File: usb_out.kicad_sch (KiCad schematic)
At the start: 31 parts, among them J6 USB_C_Receptacle_USB2.0, Q22 2N7002, U12 SY8105, U13 LM75B, U14 INA219AxD

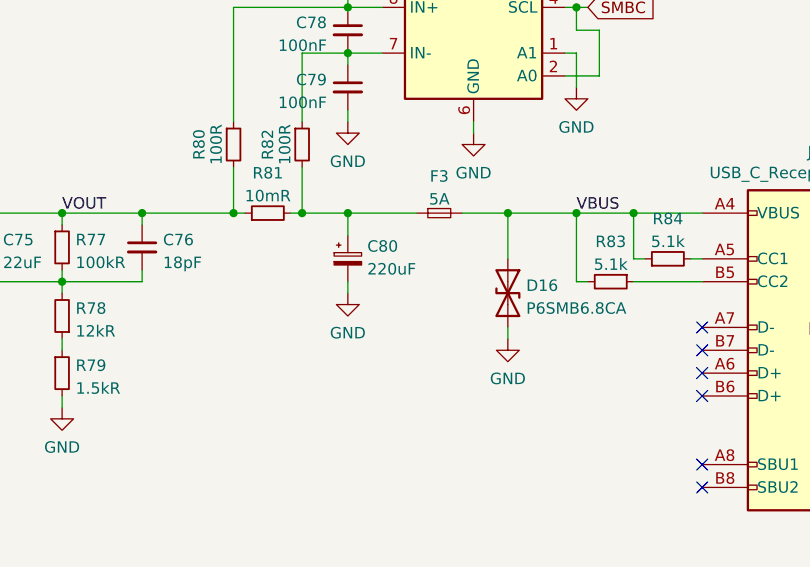
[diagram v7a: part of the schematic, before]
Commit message: Add more voltage rail LEDs
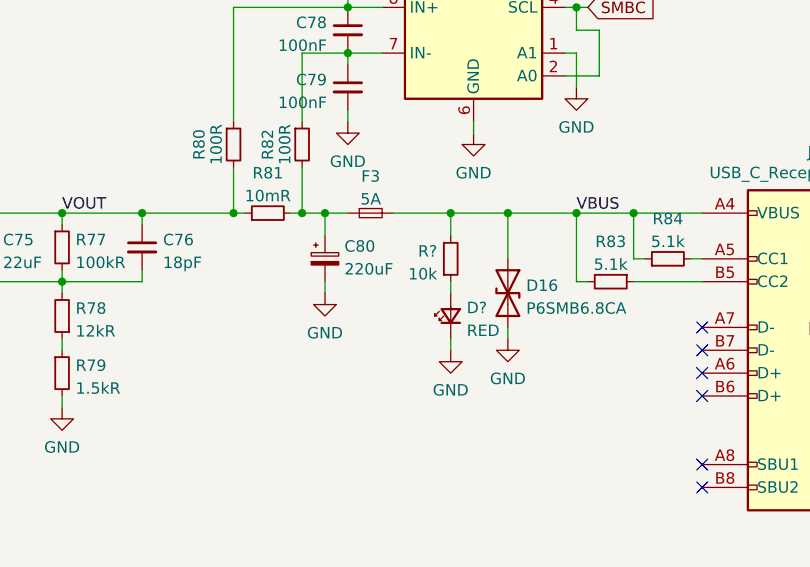
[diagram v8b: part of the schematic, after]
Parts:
- added D?: RED, LED_SMD:LED_0603_1608Metric, symbol Device:LED_Small
- added R?: 10k, Resistor_SMD:R_0402_1005Metric, symbol Device:R_Small
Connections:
- net GND: now also D?.1 (K)
- net VBUS: now also R?.2
- new net: D?.2 (A), R?.1
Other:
- moved on the sheet: C80, F3
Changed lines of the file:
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@@
   (junction (at 179.07 66.04) (diameter 0) (color 0 0 0 0)
   )
+  (junction (at 158.75 66.04) (diameter 0) (color 0 0 0 0)
+  )
   (junction (at 115.57 66.04) (diameter 0) (color 0 0 0 0)
   )
@@
   (junction (at 134.62 66.04) (diameter 0) (color 0 0 0 0)
   )
-  (junction (at 147.32 66.04) (diameter 0) (color 0 0 0 0)
-  )
   (junction (at 161.29 34.29) (diameter 0) (color 0 0 0 0)
   )
@@
   )
   (junction (at 97.79 66.04) (diameter 0) (color 0 0 0 0)
+  )
+  (junction (at 144.78 66.04) (diameter 0) (color 0 0 0 0)
   )
   (junction (at 209.55 113.03) (diameter 0) (color 0 0 0 0)
@@
     (stroke (width 0) (type default) (color 0 0 0 0))
   )
-  (wire (pts (xy 147.32 73.66) (xy 147.32 74.93))
+  (wire (pts (xy 144.78 73.66) (xy 144.78 74.93))
     (stroke (width 0) (type default) (color 0 0 0 0))
   )
@@
     (stroke (width 0) (type default) (color 0 0 0 0))
   )
-  (wire (pts (xy 147.32 66.04) (xy 154.94 66.04))
-    (stroke (width 0) (type default) (color 0 0 0 0))
-  )
   (wire (pts (xy 52.07 66.04) (xy 53.34 66.04))
     (stroke (width 0) (type default) (color 0 0 0 0))
@@
     (stroke (width 0) (type default) (color 0 0 0 0))
   )
+  (wire (pts (xy 158.75 66.04) (xy 165.1 66.04))
+    (stroke (width 0) (type default) (color 0 0 0 0))
+  )
   (wire (pts (xy 172.72 45.72) (xy 172.72 43.18))
     (stroke (width 0) (type default) (color 0 0 0 0))
@@
     (stroke (width 0) (type default) (color 0 0 0 0))
   )
-  (wire (pts (xy 142.24 66.04) (xy 147.32 66.04))
+  (wire (pts (xy 142.24 66.04) (xy 144.78 66.04))
     (stroke (width 0) (type default) (color 0 0 0 0))
   )
@@
     (stroke (width 0) (type default) (color 0 0 0 0))
   )
-  (wire (pts (xy 160.02 66.04) (xy 165.1 66.04))
+  (wire (pts (xy 152.4 66.04) (xy 158.75 66.04))
     (stroke (width 0) (type default) (color 0 0 0 0))
   )
@@
     (stroke (width 0) (type default) (color 0 0 0 0))
   )
+  (wire (pts (xy 158.75 73.66) (xy 158.75 74.93))
+    (stroke (width 0) (type default) (color 0 0 0 0))
+  )
   (wire (pts (xy 158.75 34.29) (xy 161.29 34.29))
     (stroke (width 0) (type default) (color 0 0 0 0))
@@
     (stroke (width 0) (type default) (color 0 0 0 0))
   )
-  (wire (pts (xy 147.32 66.04) (xy 147.32 68.58))
+  (wire (pts (xy 144.78 66.04) (xy 144.78 68.58))
     (stroke (width 0) (type default) (color 0 0 0 0))
   )
@@
     (stroke (width 0) (type default) (color 0 0 0 0))
   )
+  (wire (pts (xy 158.75 80.01) (xy 158.75 81.28))
+    (stroke (width 0) (type default) (color 0 0 0 0))
+  )
   (wire (pts (xy 147.32 41.91) (xy 147.32 43.18))
     (stroke (width 0) (type default) (color 0 0 0 0))
@@
     (stroke (width 0) (type default) (color 0 0 0 0))
   )
+  (wire (pts (xy 158.75 68.58) (xy 158.75 66.04))
+    (stroke (width 0) (type default) (color 0 0 0 0))
+  )
   (wire (pts (xy 115.57 66.04) (xy 124.46 66.04))
     (stroke (width 0) (type default) (color 0 0 0 0))
@@
   )
   (wire (pts (xy 172.72 48.26) (xy 171.45 48.26))
+    (stroke (width 0) (type default) (color 0 0 0 0))
+  )
+  (wire (pts (xy 144.78 66.04) (xy 147.32 66.04))
     (stroke (width 0) (type default) (color 0 0 0 0))
   )
@@
     (pin "1")
   )
-  (symbol (lib_id "Device:Fuse_Small") (at 157.48 66.04 0) (unit 1)
-    (in_bom yes) (on_board yes) (fields_autoplaced)
-    (property "Reference" "F3" (id 0) (at 157.48 61.9592 0))
-    (property "Value" "5A" (id 1) (at 157.48 64.4961 0))
-    (property "Footprint" "Fuse:Fuse_1206_3216Metric" (id 2) (at 157.48 66.04 0)
-      (effects (font (size 1.27 1.27)) hide)
-    )
-    (property "Datasheet" "https://datasheet.lcsc.com/lcsc/1912111437_HOLLY-12T-050L2_C377290.pdf" (id 3) (at 157.48 66.04 0)
-      (effects (font (size 1.27 1.27)) hide)
-    )
-    (property "LCSC" "C377290" (id 4) (at 157.48 66.04 0)
+  (symbol (lib_id "Device:Fuse_Small") (at 149.86 66.04 0) (unit 1)
+    (in_bom yes) (on_board yes) (fields_autoplaced)
+    (property "Reference" "F3" (id 0) (at 149.86 61.9592 0))
+    (property "Value" "5A" (id 1) (at 149.86 64.4961 0))
+    (property "Footprint" "Fuse:Fuse_1206_3216Metric" (id 2) (at 149.86 66.04 0)
+      (effects (font (size 1.27 1.27)) hide)
+    )
+    (property "Datasheet" "https://datasheet.lcsc.com/lcsc/1912111437_HOLLY-12T-050L2_C377290.pdf" (id 3) (at 149.86 66.04 0)
+      (effects (font (size 1.27 1.27)) hide)
+    )
+    (property "LCSC" "C377290" (id 4) (at 149.86 66.04 0)
       (effects (font (size 1.27 1.27)) hide)
     )
@@
     (pin "1")
   )
-  (symbol (lib_id "power:GND") (at 147.32 74.93 0) (unit 1)
-    (in_bom yes) (on_board yes) (fields_autoplaced)
-    (property "Reference" "#PWR0234" (id 0) (at 147.32 81.28 0)
-      (effects (font (size 1.27 1.27)) hide)
-    )
-    (property "Value" "GND" (id 1) (at 147.32 79.3734 0))
-    (property "Footprint" "" (id 2) (at 147.32 74.93 0)
-      (effects (font (size 1.27 1.27)) hide)
-    )
-    (property "Datasheet" "" (id 3) (at 147.32 74.93 0)
+  (symbol (lib_id "power:GND") (at 144.78 74.93 0) (unit 1)
+    (in_bom yes) (on_board yes) (fields_autoplaced)
+    (property "Reference" "#PWR0234" (id 0) (at 144.78 81.28 0)
+      (effects (font (size 1.27 1.27)) hide)
+    )
+    (property "Value" "GND" (id 1) (at 144.78 79.3734 0))
+    (property "Footprint" "" (id 2) (at 144.78 74.93 0)
+      (effects (font (size 1.27 1.27)) hide)
+    )
+    (property "Datasheet" "" (id 3) (at 144.78 74.93 0)
       (effects (font (size 1.27 1.27)) hide)
     )
@@
     (pin "1")
   )
+  (symbol (lib_id "Device:R_Small") (at 158.75 71.12 0) (mirror x) (unit 1)
+    (in_bom yes) (on_board yes) (fields_autoplaced)
+    (property "Reference" "R?" (id 0) (at 157.2515 70.2853 0)
+      (effects (font (size 1.27 1.27)) (justify right))
+    )
+    (property "Value" "10k" (id 1) (at 157.2515 72.8222 0)
+      (effects (font (size 1.27 1.27)) (justify right))
+    )
+    (property "Footprint" "Resistor_SMD:R_0402_1005Metric" (id 2) (at 158.75 71.12 0)
+      (effects (font (size 1.27 1.27)) hide)
+    )
+    (property "Datasheet" "~" (id 3) (at 158.75 71.12 0)
+      (effects (font (size 1.27 1.27)) hide)
+    )
+    (property "LCSC" "C25744" (id 4) (at 158.75 71.12 0)
+      (effects (font (size 1.27 1.27)) hide)
+    )
+    (pin "1")
+    (pin "2")
+  )
   (symbol (lib_id "power:GND") (at 139.7 34.29 0) (unit 1)
     (in_bom yes) (on_board yes) (fields_autoplaced)
@@
     (pin "2")
   )
+  (symbol (lib_id "Device:LED_Small") (at 158.75 77.47 90) (unit 1)
+    (in_bom yes) (on_board yes) (fields_autoplaced)
+    (property "Reference" "D?" (id 0) (at 160.528 76.5718 90)
+      (effects (font (size 1.27 1.27)) (justify right))
+    )
+    (property "Value" "RED" (id 1) (at 160.528 79.1087 90)
+      (effects (font (size 1.27 1.27)) (justify right))
+    )
+    (property "Footprint" "LED_SMD:LED_0603_1608Metric" (id 2) (at 158.75 77.47 90)
+      (effects (font (size 1.27 1.27)) hide)
+    )
+    (property "Datasheet" "~" (id 3) (at 158.75 77.47 90)
+      (effects (font (size 1.27 1.27)) hide)
+    )
+    (property "LCSC" "C2286" (id 4) (at 158.75 77.47 0)
+      (effects (font (size 1.27 1.27)) hide)
+    )
+    (pin "1")
+    (pin "2")
+  )
   (symbol (lib_id "Device:C_Small") (at 156.21 34.29 270) (mirror x) (unit 1)
     (in_bom yes) (on_board yes)
@@
     (pin "2")
   )
-  (symbol (lib_id "Device:C_Polarized_Small") (at 147.32 71.12 0) (unit 1)
-    (in_bom yes) (on_board yes) (fields_autoplaced)
-    (property "Reference" "C80" (id 0) (at 149.479 69.7392 0)
-      (effects (font (size 1.27 1.27)) (justify left))
-    )
-    (property "Value" "220uF" (id 1) (at 149.479 72.2761 0)
-      (effects (font (size 1.27 1.27)) (justify left))
-    )
-    (property "Footprint" "Capacitor_SMD:CP_Elec_6.3x7.7" (id 2) (at 147.32 71.12 0)
-      (effects (font (size 1.27 1.27)) hide)
-    )
-    (property "Datasheet" "https://datasheet.lcsc.com/lcsc/1912111437_Nichicon-UCM1E221MCL1GS_C340768.pdf" (id 3) (at 147.32 71.12 0)
-      (effects (font (size 1.27 1.27)) hide)
-    )
-    (property "LCSC" "C340768" (id 4) (at 147.32 71.12 0)
-      (effects (font (size 1.27 1.27)) hide)
-    )
+  (symbol (lib_id "power:GND") (at 158.75 81.28 0) (unit 1)
+    (in_bom yes) (on_board yes) (fields_autoplaced)
+    (property "Reference" "#PWR?" (id 0) (at 158.75 87.63 0)
+      (effects (font (size 1.27 1.27)) hide)
+    )
+    (property "Value" "GND" (id 1) (at 158.75 85.7234 0))
+    (property "Footprint" "" (id 2) (at 158.75 81.28 0)
+      (effects (font (size 1.27 1.27)) hide)
+    )
+    (property "Datasheet" "" (id 3) (at 158.75 81.28 0)
+      (effects (font (size 1.27 1.27)) hide)
+    )
+    (pin "1")
+  )
+  (symbol (lib_id "Device:C_Polarized_Small") (at 144.78 71.12 0) (unit 1)
+    (in_bom yes) (on_board yes) (fields_autoplaced)
+    (property "Reference" "C80" (id 0) (at 146.939 69.7392 0)
+      (effects (font (size 1.27 1.27)) (justify left))
+    )
+    (property "Value" "220uF" (id 1) (at 146.939 72.2761 0)
+      (effects (font (size 1.27 1.27)) (justify left))
+    )
+    (property "Footprint" "Capacitor_SMD:CP_Elec_6.3x7.7" (id 2) (at 144.78 71.12 0)
+      (effects (font (size 1.27 1.27)) hide)
+    )
+    (property "Datasheet" "https://datasheet.lcsc.com/lcsc/1912111437_Nichicon-UCM1E221MCL1GS_C340768.pdf" (id 3) (at 144.78 71.12 0)
+      (effects (font (size 1.27 1.27)) hide)
+    )
+    (property "LCSC" "C340768" (id 4) (at 144.78 71.12 0)
+      (effects (font (size 1.27 1.27)) hide)
+    )
